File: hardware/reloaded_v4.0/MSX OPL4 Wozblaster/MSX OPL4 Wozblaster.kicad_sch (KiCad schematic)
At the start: 21 parts, among them IC1 GAL16V8D, IC5 YMF278B-F, IC6 AM29F016B-120EC, Q1 33.8688, U1 CY62167ELL, U2 UDA1334MOD

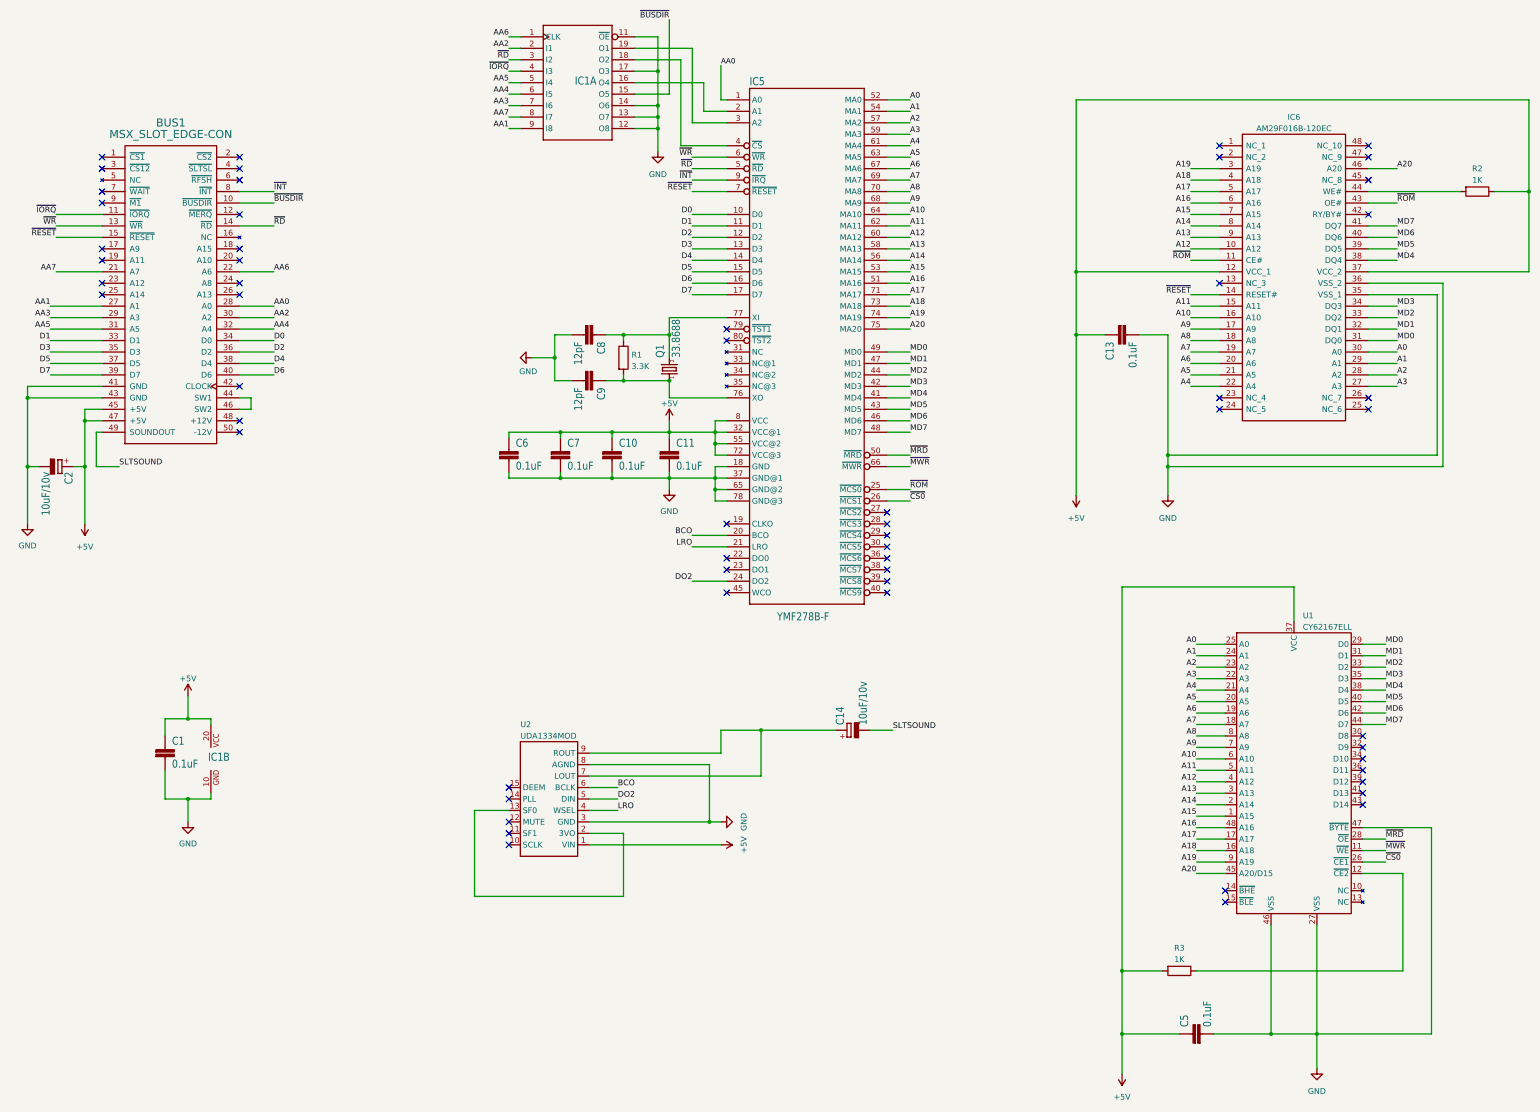
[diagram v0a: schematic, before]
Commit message: Footprint adjustments, README, small fixes
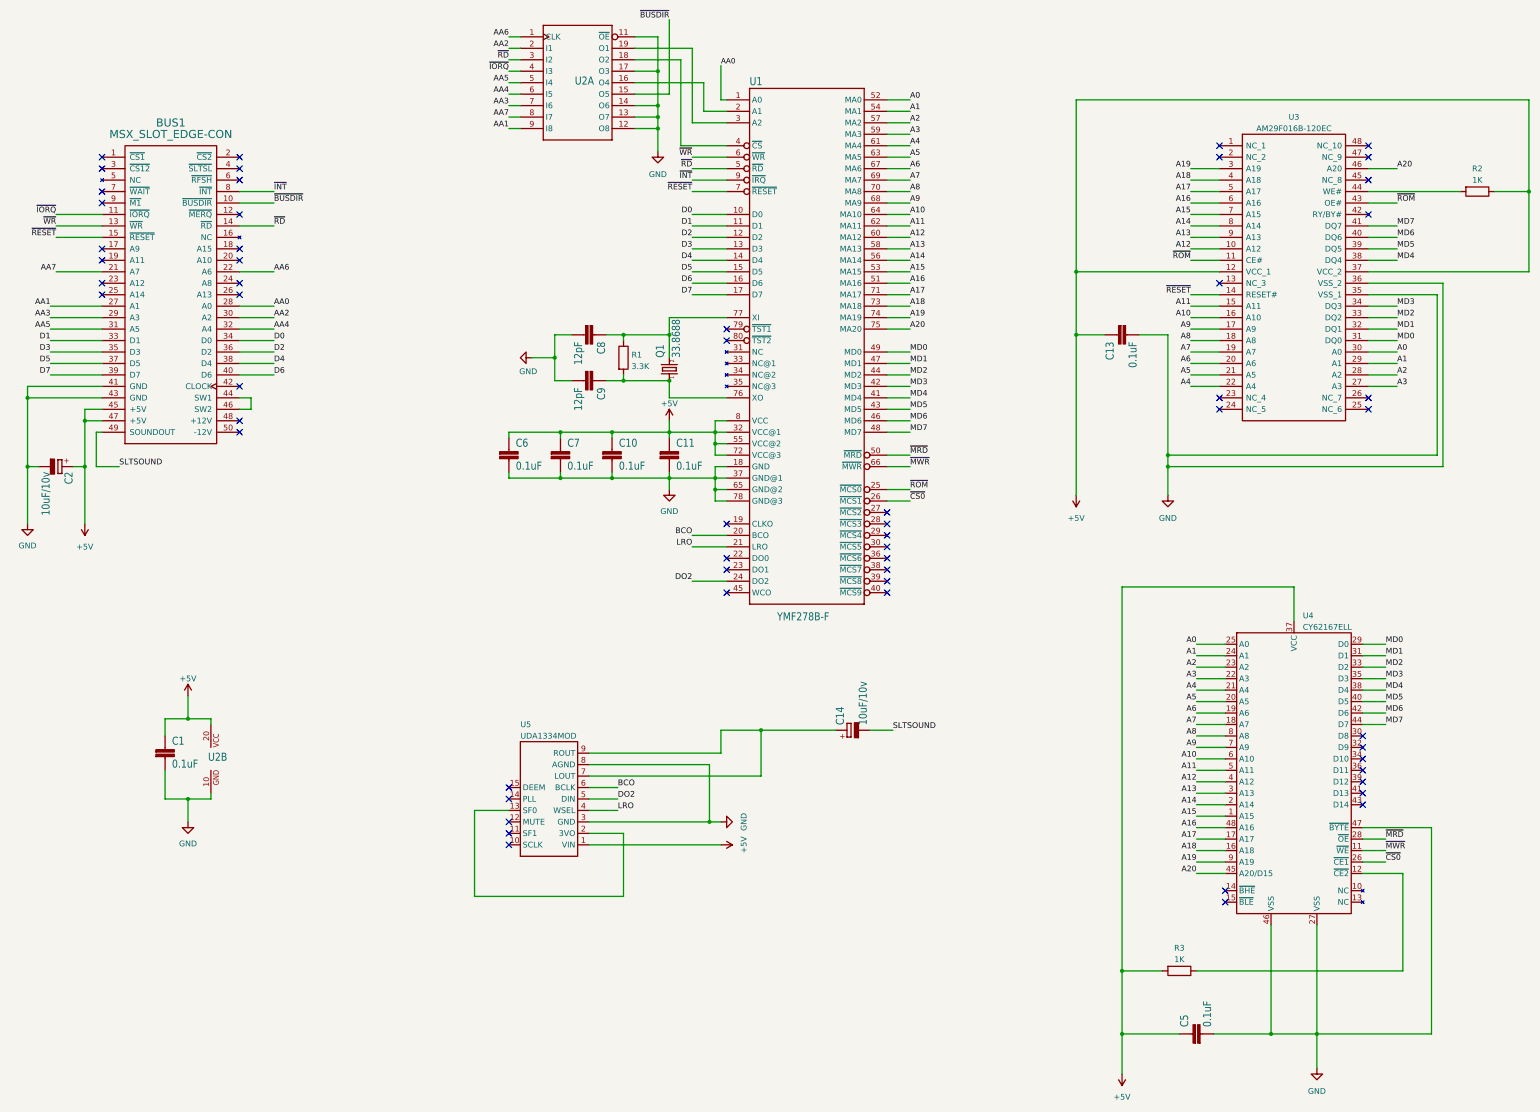
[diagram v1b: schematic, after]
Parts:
- U3: renamed from IC6; footprint CRISAG:SOP50P2000X120-48N -> MSX OPL4 Wozblaster:SOP50P2000X120-48N
- U4: renamed from U1; footprint (none) -> MSX OPL4 Wozblaster:SOP50P2000X120-48N
- U5: renamed from U2; footprint CRISAG:UDA1334MOD -> MSX OPL4 Wozblaster:UDA1334MOD
- renumbered IC5 to U1, IC1 to U2
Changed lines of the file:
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@@
   (symbol (lib_id "CRISAG:YMF278B-F") (at 314.96 144.78 0) (unit 1)
     (in_bom yes) (on_board yes) (dnp no)
-    (property "Reference" "IC5" (at 302.26 90.932 0)
+    (property "Reference" "U1" (at 302.26 90.932 0)
       (effects (font (size 1.778 1.5113)) (justify left bottom))
     )
@@
       (project "MSX OPL4 Wozblaster"
         (path "/319085e4-dbf0-404d-8e32-9614d4e1a0c6"
-          (reference "IC5") (unit 1)
+          (reference "U1") (unit 1)
         )
       )
@@
   (symbol (lib_id "CRISAG:UDA1334_MOD") (at 257.81 248.92 90) (unit 1)
     (in_bom yes) (on_board yes) (dnp no)
-    (property "Reference" "U2" (at 251.46 232.41 90)
+    (property "Reference" "U5" (at 251.46 232.41 90)
       (effects (font (size 1.27 1.27)) (justify right))
     )
@@
       (effects (font (size 1.27 1.27)) (justify right))
     )
-    (property "Footprint" "CRISAG:UDA1334MOD" (at 257.81 248.92 0)
+    (property "Footprint" "MSX OPL4 Wozblaster:UDA1334MOD" (at 257.81 248.92 0)
       (effects (font (size 1.27 1.27)) hide)
     )
@@
       (project "MSX OPL4 Wozblaster"
         (path "/319085e4-dbf0-404d-8e32-9614d4e1a0c6"
-          (reference "U2") (unit 1)
+          (reference "U5") (unit 1)
         )
       )
@@
   (symbol (lib_id "CY62167:CY62167ELL-45ZXI") (at 422.91 245.11 0) (unit 1)
     (in_bom yes) (on_board yes) (dnp no) (fields_autoplaced)
-    (property "Reference" "U1" (at 424.8659 208.28 0)
+    (property "Reference" "U4" (at 424.8659 208.28 0)
       (effects (font (size 1.27 1.27)) (justify left))
     )
@@
       (effects (font (size 1.27 1.27)) (justify left))
     )
-    (property "Footprint" "" (at 417.83 232.41 0)
+    (property "Footprint" "MSX OPL4 Wozblaster:SOP50P2000X120-48N" (at 417.83 232.41 0)
       (effects (font (size 1.27 1.27)) hide)
     )
     (property "Datasheet" "" (at 417.83 232.41 0)
+      (effects (font (size 1.27 1.27)) hide)
+    )
+    (property "Sim.Device" "I" (at 422.91 245.11 0)
+      (effects (font (size 1.27 1.27)) hide)
+    )
+    (property "Sim.Type" "DC" (at 422.91 245.11 0)
+      (effects (font (size 1.27 1.27)) hide)
+    )
+    (property "Sim.Pins" "1=+ 2=-" (at 422.91 245.11 0)
+      (effects (font (size 1.27 1.27)) hide)
+    )
+    (property "Sim.Params" "dc=\"\"" (at 422.91 245.11 0)
       (effects (font (size 1.27 1.27)) hide)
     )
@@
       (project "MSX OPL4 Wozblaster"
         (path "/319085e4-dbf0-404d-8e32-9614d4e1a0c6"
-          (reference "U1") (unit 1)
+          (reference "U4") (unit 1)
         )
       )
@@
   (symbol (lib_name "GAL16V8P3_1") (lib_id "CRISAG:GAL16V8P3") (at 264.16 90.17 0) (unit 1)
     (in_bom yes) (on_board yes) (dnp no)
-    (property "Reference" "IC1" (at 263.525 90.805 0)
+    (property "Reference" "U2" (at 263.525 90.805 0)
       (effects (font (size 1.778 1.5113)) (justify left bottom))
     )
@@
       (project "MSX OPL4 Wozblaster"
         (path "/319085e4-dbf0-404d-8e32-9614d4e1a0c6"
-          (reference "IC1") (unit 1)
+          (reference "U2") (unit 1)
         )
       )
@@
   (symbol (lib_id "CRISAG:GAL16V8P3") (at 182.88 240.03 0) (unit 2)
     (in_bom yes) (on_board yes) (dnp no)
-    (property "Reference" "IC1" (at 182.245 240.665 0)
+    (property "Reference" "U2" (at 182.245 240.665 0)
       (effects (font (size 1.778 1.5113)) (justify left bottom))
     )
@@
       (project "MSX OPL4 Wozblaster"
         (path "/319085e4-dbf0-404d-8e32-9614d4e1a0c6"
-          (reference "IC1") (unit 2)
+          (reference "U2") (unit 2)
         )
       )
@@
   (symbol (lib_id "CRISAG:AM29F016B-120EC") (at 406.4 104.14 0) (unit 1)
     (in_bom yes) (on_board yes) (dnp no) (fields_autoplaced)
-    (property "Reference" "IC6" (at 422.91 97.79 0)
+    (property "Reference" "U3" (at 422.91 97.79 0)
       (effects (font (size 1.27 1.27)))
     )
@@
       (effects (font (size 1.27 1.27)))
     )
-    (property "Footprint" "CRISAG:SOP50P2000X120-48N" (at 435.61 101.6 0)
+    (property "Footprint" "MSX OPL4 Wozblaster:SOP50P2000X120-48N" (at 435.61 101.6 0)
       (effects (font (size 1.27 1.27)) (justify left) hide)
     )
@@
       (project "MSX OPL4 Wozblaster"
         (path "/319085e4-dbf0-404d-8e32-9614d4e1a0c6"
-          (reference "IC6") (unit 1)
-        )
-      )
+          (reference "U3") (unit 1)
+        )
+      )
